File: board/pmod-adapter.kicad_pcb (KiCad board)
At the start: 2 copper layers, 2 parts

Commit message: Lots of updates.
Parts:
- added PH3: PMOD-Device-x2-Type-XHS, pmod-conn_6x2:pmod_pin_array_6x2_hs, B.Cu at (50.8, 76.2)
- added PX3: PMOD-Device-x2-Type-XADC, pmod-conn_6x2:pmod_pin_array_6x2_xadc, F.Cu at (40.6, 71.1)
- PH1: footprint pmod-conn_6x2:pmod_pin_array_6x2 -> pmod-conn_6x2:pmod_pin_array_6x2_hs
- PX1: footprint pmod-conn_6x2:pmod_pin_array_6x2 -> pmod-conn_6x2:pmod_pin_array_6x2_xadc
- moved PH1 129.6 mm to (50.8, 30.5)
- moved PX1 129.6 mm to (40.6, 30.5)
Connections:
- PH1 pad 11: /GND22 -> /GND
- PH1 pad 5: /GND21 -> /GND
- PX1 pad 11: /GND22 -> /GND
- PX1 pad 5: /GND21 -> /GND
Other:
- board outline added: 20.3 x 86.4 mm
- board text added: "Break Line 1"

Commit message: Small updates.
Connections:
- PH1 pad 11: /GND -> /GND2
- PH1 pad 5: /GND -> /GND2
- PH3 pad 11: /GND -> /GND3
- PH3 pad 5: /GND -> /GND3
- PX1 pad 11: /GND -> /GND2
- PX1 pad 5: /GND -> /GND2
- PX3 pad 11: /GND -> /GND3
- PX3 pad 5: /GND -> /GND3
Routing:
- added copper zone on B.Cu, net /GND1
- added copper zone on B.Cu, net /GND2
- added copper zone on B.Cu, net /GND3

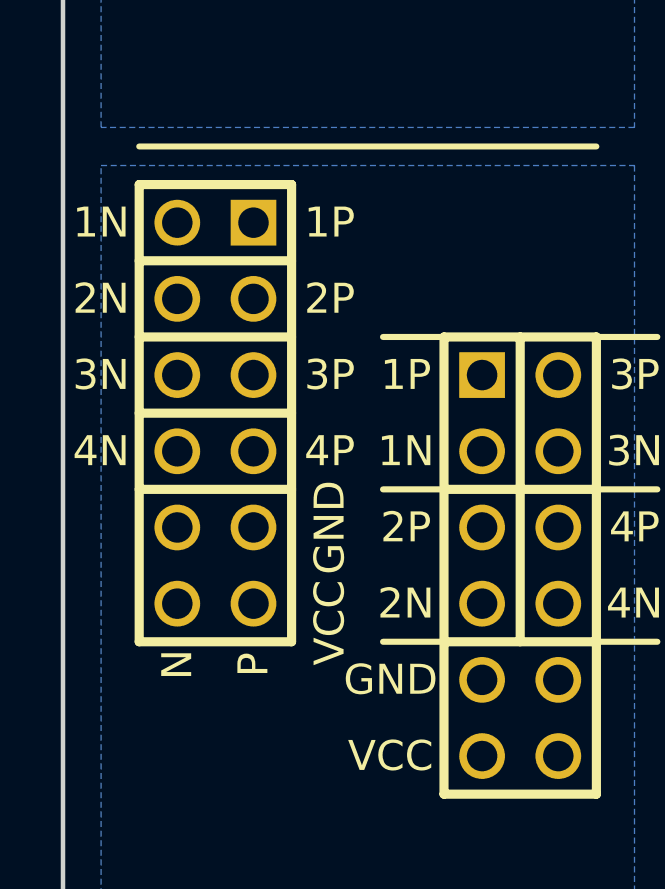
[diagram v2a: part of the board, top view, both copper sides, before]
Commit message: Working on getting the Numato spacing right.
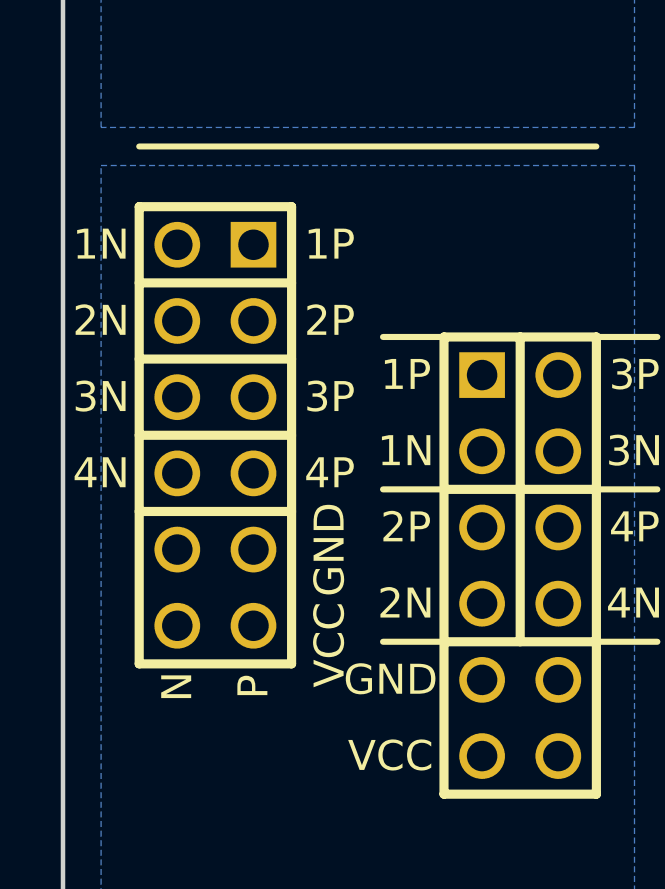
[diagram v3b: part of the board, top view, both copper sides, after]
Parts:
- moved PX3 0.74 mm to (40.6, 71.9)
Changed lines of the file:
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@@
     (links 55)
     (no_connects 55)
-    (area 35.484999 21.514999 55.955001 108.025001)
+    (area 20.891207 18.824999 83.151428 110.715001)
     (thickness 1.6)
-    (drawings 17)
+    (drawings 18)
     (tracks 0)
     (zones 0)
@@
   )
   (module pmod-conn_6x2:pmod_pin_array_6x2_xadc (layer F.Cu)
-    (at 40.64 50.8)
+    (at 40.64 51.1683)
     (descr "QMOD Pin Header 2 x 6 pins")
     (tags CONN)
@@
   )
   (module pmod-conn_6x2:pmod_pin_array_6x2_xadc (layer F.Cu)
-    (at 40.64 71.12)
+    (at 40.64 71.8566)
     (descr "QMOD Pin Header 2 x 6 pins")
     (tags CONN)
@@
   )
   (module pmod-conn_6x2:pmod_pin_array_6x2_xadc (layer F.Cu)
-    (at 40.64 91.44)
+    (at 40.64 92.5449)
     (descr "QMOD Pin Header 2 x 6 pins")
     (tags CONN)
@@
     )
   )
+  (dimension 7.9883 (width 0.0001) (layer Eco1.User)
+    (gr_text "0.3145 in" (at 33.5398 82.20075 270) (layer Eco1.User)
+      (effects (font (size 1.5 1.5) (thickness 0.0001)))
+    )
+    (feature1 (pts (xy 39.37 86.1949) (xy 32.7896 86.1949)))
+    (feature2 (pts (xy 39.37 78.2066) (xy 32.7896 78.2066)))
+    (crossbar (pts (xy 34.29 78.2066) (xy 34.29 86.1949)))
+    (arrow1a (pts (xy 34.29 86.1949) (xy 33.703579 85.068396)))
+    (arrow1b (pts (xy 34.29 86.1949) (xy 34.876421 85.068396)))
+    (arrow2a (pts (xy 34.29 78.2066) (xy 33.703579 79.333104)))
+    (arrow2b (pts (xy 34.29 78.2066) (xy 34.876421 79.333104)))
+  )
+  (dimension 7.9883 (width 0.0001) (layer Eco1.User)
+    (gr_text "0.3145 in" (at 33.5398 61.51245 270) (layer Eco1.User)
+      (effects (font (size 1.5 1.5) (thickness 0.0001)))
+    )
+    (feature1 (pts (xy 39.37 65.5066) (xy 32.7896 65.5066)))
+    (feature2 (pts (xy 39.37 57.5183) (xy 32.7896 57.5183)))
+    (crossbar (pts (xy 34.29 57.5183) (xy 34.29 65.5066)))
+    (arrow1a (pts (xy 34.29 65.5066) (xy 33.703579 64.380096)))
+    (arrow1b (pts (xy 34.29 65.5066) (xy 34.876421 64.380096)))
+    (arrow2a (pts (xy 34.29 57.5183) (xy 33.703579 58.644804)))
+    (arrow2b (pts (xy 34.29 57.5183) (xy 34.876421 58.644804)))
+  )
+  (dimension 7.9883 (width 0.00254) (layer Eco1.User)
+    (gr_text "7.988 mm" (at 26.67692 40.82415 270) (layer Eco1.User)
+      (effects (font (size 1.5 1.5) (thickness 0.00254)))
+    )
+    (feature1 (pts (xy 39.37 44.8183) (xy 25.92184 44.8183)))
+    (feature2 (pts (xy 39.37 36.83) (xy 25.92184 36.83)))
+    (crossbar (pts (xy 27.432 36.83) (xy 27.432 44.8183)))
+    (arrow1a (pts (xy 27.432 44.8183) (xy 26.845579 43.691796)))
+    (arrow1b (pts (xy 27.432 44.8183) (xy 28.018421 43.691796)))
+    (arrow2a (pts (xy 27.432 36.83) (xy 26.845579 37.956504)))
+    (arrow2b (pts (xy 27.432 36.83) (xy 28.018421 37.956504)))
+  )
   (gr_line (start 35.56 62.23) (end 67.945 62.23) (layer Eco1.User) (width 0.2))
   (gr_line (start 67.945 39.37) (end 35.56 39.37) (layer Eco1.User) (width 0.2))
@@
   (gr_line (start 35.56 21.59) (end 55.88 21.59) (layer F.SilkS) (width 0.2))
   (gr_line (start 38.1 62.23) (end 53.34 62.23) (layer F.SilkS) (width 0.2))
-  (dimension 7.62 (width 0.3) (layer Eco1.User)
+  (dimension 7.62 (width 0.00254) (layer Eco1.User)
     (gr_text "0.3000 in" (at 64.85 87.602222 270) (layer Eco1.User)
-      (effects (font (size 1.5 1.5) (thickness 0.3)))
+      (effects (font (size 1.5 1.5) (thickness 0.00254)))
     )
     (feature1 (pts (xy 53.34 91.412222) (xy 66.2 91.412222)))
@@
     (arrow2b (pts (xy 63.5 83.792222) (xy 64.086421 84.918726)))
   )
-  (dimension 5.08 (width 0.3) (layer Eco1.User)
-    (gr_text "0.2000 in" (at 31.67 81.28 270) (layer Eco1.User)
-      (effects (font (size 1.5 1.5) (thickness 0.3)))
-    )
-    (feature1 (pts (xy 38.1 83.82) (xy 30.32 83.82)))
-    (feature2 (pts (xy 38.1 78.74) (xy 30.32 78.74)))
-    (crossbar (pts (xy 33.02 78.74) (xy 33.02 83.82)))
-    (arrow1a (pts (xy 33.02 83.82) (xy 32.433579 82.693496)))
-    (arrow1b (pts (xy 33.02 83.82) (xy 33.606421 82.693496)))
-    (arrow2a (pts (xy 33.02 78.74) (xy 32.433579 79.866504)))
-    (arrow2b (pts (xy 33.02 78.74) (xy 33.606421 79.866504)))
-  )
-  (dimension 5.08 (width 0.3) (layer Eco1.User)
-    (gr_text "0.2000 in" (at 31.67 60.96 270) (layer Eco1.User)
-      (effects (font (size 1.5 1.5) (thickness 0.3)))
-    )
-    (feature1 (pts (xy 38.1 63.5) (xy 30.32 63.5)))
-    (feature2 (pts (xy 38.1 58.42) (xy 30.32 58.42)))
-    (crossbar (pts (xy 33.02 58.42) (xy 33.02 63.5)))
-    (arrow1a (pts (xy 33.02 63.5) (xy 32.433579 62.373496)))
-    (arrow1b (pts (xy 33.02 63.5) (xy 33.606421 62.373496)))
-    (arrow2a (pts (xy 33.02 58.42) (xy 32.433579 59.546504)))
-    (arrow2b (pts (xy 33.02 58.42) (xy 33.606421 59.546504)))
-  )
-  (dimension 7.62 (width 0.3) (layer Eco1.User)
+  (dimension 7.62 (width 0.00254) (layer Eco1.User)
     (gr_text "0.3000 in" (at 64.85 64.719342 270) (layer Eco1.User)
-      (effects (font (size 1.5 1.5) (thickness 0.3)))
+      (effects (font (size 1.5 1.5) (thickness 0.00254)))
     )
     (feature1 (pts (xy 53.34 68.529342) (xy 66.2 68.529342)))
@@
     (arrow2b (pts (xy 63.5 60.909342) (xy 64.086421 62.035846)))
   )
-  (dimension 5.08 (width 0.3) (layer Eco1.User)
-    (gr_text "0.2000 in" (at 31.67 40.64 270) (layer Eco1.User)
-      (effects (font (size 1.5 1.5) (thickness 0.3)))
-    )
-    (feature1 (pts (xy 38.1 43.18) (xy 30.32 43.18)))
-    (feature2 (pts (xy 38.1 38.1) (xy 30.32 38.1)))
-    (crossbar (pts (xy 33.02 38.1) (xy 33.02 43.18)))
-    (arrow1a (pts (xy 33.02 43.18) (xy 32.433579 42.053496)))
-    (arrow1b (pts (xy 33.02 43.18) (xy 33.606421 42.053496)))
-    (arrow2a (pts (xy 33.02 38.1) (xy 32.433579 39.226504)))
-    (arrow2b (pts (xy 33.02 38.1) (xy 33.606421 39.226504)))
-  )
-  (dimension 7.62 (width 0.3) (layer Eco1.User)
+  (dimension 7.9883 (width 0.0001) (layer Eco1.User)
+    (gr_text "0.3145 in" (at 33.5398 40.82415 270) (layer Eco1.User)
+      (effects (font (size 1.5 1.5) (thickness 0.0001)))
+    )
+    (feature1 (pts (xy 39.37 44.8183) (xy 32.7896 44.8183)))
+    (feature2 (pts (xy 39.37 36.83) (xy 32.7896 36.83)))
+    (crossbar (pts (xy 34.29 36.83) (xy 34.29 44.8183)))
+    (arrow1a (pts (xy 34.29 44.8183) (xy 33.703579 43.691796)))
+    (arrow1b (pts (xy 34.29 44.8183) (xy 34.876421 43.691796)))
+    (arrow2a (pts (xy 34.29 36.83) (xy 33.703579 37.956504)))
+    (arrow2b (pts (xy 34.29 36.83) (xy 34.876421 37.956504)))
+  )
+  (dimension 7.62 (width 0.00254) (layer Eco1.User)
     (gr_text "0.3000 in" (at 64.85 41.91 270) (layer Eco1.User)
-      (effects (font (size 1.5 1.5) (thickness 0.3)))
+      (effects (font (size 1.5 1.5) (thickness 0.00254)))
     )
     (feature1 (pts (xy 53.34 45.72) (xy 66.2 45.72)))

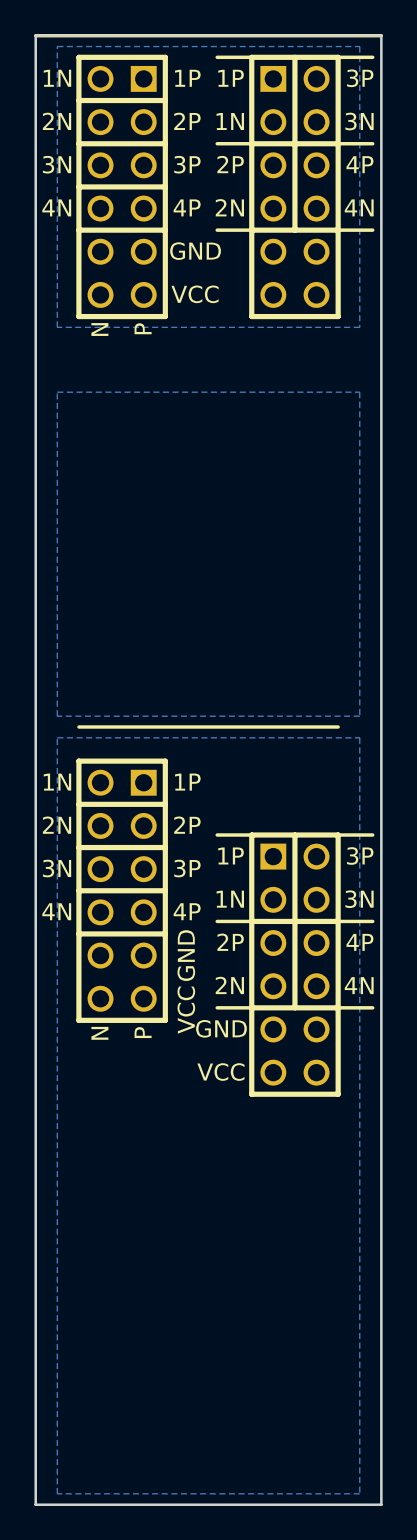
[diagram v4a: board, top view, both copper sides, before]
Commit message: Rework the schematic to make board easier to route.
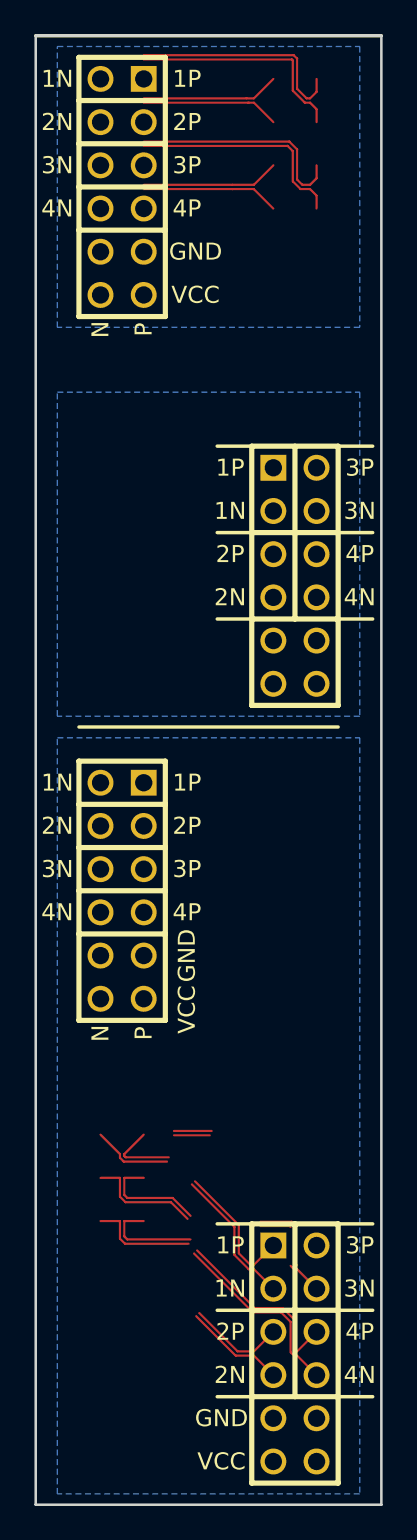
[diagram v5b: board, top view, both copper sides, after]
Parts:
- removed PH1, PH3: PMOD-Device-x2-Type-XHS, pmod-conn_6x2:pmod_pin_array_6x2_hs
- added PH2: PMOD-Device-x2-Type-XHS, pmod-conn_6x2:pmod_pin_array_6x2_hs, B.Cu at (50.8, 53.3)
- added PH4: PMOD-Device-x2-Type-XHS, pmod-conn_6x2:pmod_pin_array_6x2_hs, B.Cu at (50.8, 99.1)
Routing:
- net /J14_P: track 0.00 -> 13.2 mm
- net /J13_N: track 0.00 -> 13.2 mm
- net /J14_N: track 0.00 -> 13.2 mm
- net /J13_P: track 0.00 -> 13.2 mm
- net /J41_N: track 0.00 -> 13.0 mm
- net /J42_N: track 0.00 -> 12.7 mm
- net /J41_P: track 0.00 -> 12.5 mm
- net /J42_P: track 0.00 -> 12.3 mm
- net /J44_N: track 0.00 -> 11.2 mm
- net /J44_P: track 0.00 -> 11.0 mm
- net /J43_N: track 0.00 -> 10.2 mm
- net /J43_P: track 0.00 -> 8.27 mm
- net /J11_N: track 0.00 -> 8.09 mm
- net /J11_P: track 0.00 -> 8.09 mm
- net /J12_N: track 0.00 -> 8.09 mm
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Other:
- net class Default: clearance 0.2 -> 0.127; trace_width 0.25 -> 0.127; via_dia 0.6 -> 0.6096; via_drill 0.4 -> 0.3048
- rule trace_clearance: 0.2 -> 0.127
- rule trace_min: 0.2 -> 0.127
- rule via_min_drill: 0.3 -> 0.3048
- rule via_min_size: 0.4 -> 0.6096

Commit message: Routing all pairs.
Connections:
- net /GND3 renamed /GND34
- net /J11_N renamed /J1A_N
- net /J11_P renamed /J1A_P
- net /J12_N renamed /J1C_N
- net /J12_P renamed /J1C_P
- net /J13_N renamed /J1B_N
- net /J13_P renamed /J1B_P
- net /J14_N renamed /J1D_N
- net /J14_P renamed /J1D_P
- net /J21_N renamed /J2A_N
- net /J21_P renamed /J2A_P
- net /J22_N renamed /J2B_N
- net /J22_P renamed /J2B_P
- net /J23_N renamed /J2C_N
- net /J23_P renamed /J2C_P
- net /J24_N renamed /J2D_N
- net /J24_P renamed /J2D_P
- net /J31_N renamed /J3A_N
- net /J31_P renamed /J3A_P
- net /J32_N renamed /J3C_N
- net /J32_P renamed /J3C_P
- net /J33_N renamed /J3B_N
- net /J33_P renamed /J3B_P
- net /J34_N renamed /J3D_N
- net /J34_P renamed /J3D_P
- net /J41_N renamed /J4A_N
- net /J41_P renamed /J4A_P
- net /J42_N renamed /J4B_N
- net /J42_P renamed /J4B_P
- net /J43_N renamed /J4C_N
- net /J43_P renamed /J4C_P
- net /J44_N renamed /J4D_N
- net /J44_P renamed /J4D_P
- PX3 pad 12: /VCC32 -> /VCC42
- PX3 pad 6: /VCC31 -> /VCC41
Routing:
- net /J3B_N: track 0.00 -> 18.6 mm
- net /J3D_N: track 0.00 -> 18.5 mm
- net /J3B_P: track 0.00 -> 18.2 mm
- net /J3D_P: track 0.00 -> 18.1 mm
- net /J2B_N: track 0.00 -> 17.7 mm
- net /J2D_N: track 0.00 -> 17.6 mm
- net /J2B_P: track 0.00 -> 17.3 mm
- net /J2D_P: track 0.00 -> 17.2 mm
- net /J3C_N: track 0.00 -> 13.5 mm
- net /J3A_N: track 0.00 -> 13.4 mm
- net /J3C_P: track 0.00 -> 13.1 mm
- net /J3A_P: track 0.00 -> 13.0 mm
- net /J2C_N: track 0.00 -> 12.6 mm
- net /J2A_N: track 0.00 -> 12.5 mm
- net /J2C_P: track 0.00 -> 12.2 mm
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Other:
- net class LVDS_DP0.0254/0.0254 added: clearance 0.127, trace_width 0.127, via_dia 0.6096, via_drill 0.3048
